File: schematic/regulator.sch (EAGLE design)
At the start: 26 parts, among them J1 COMM, J2 STOP_LIGHT, J3 ON/OFF, J4 BATTERY, J5 DRIVER, J6 DRIVER POWER, Q1 NMOSFETSOT23, Q2 NMOSFETSOT23, Q3 NMOSFETSOT23, Q4 IRFR3607PBF

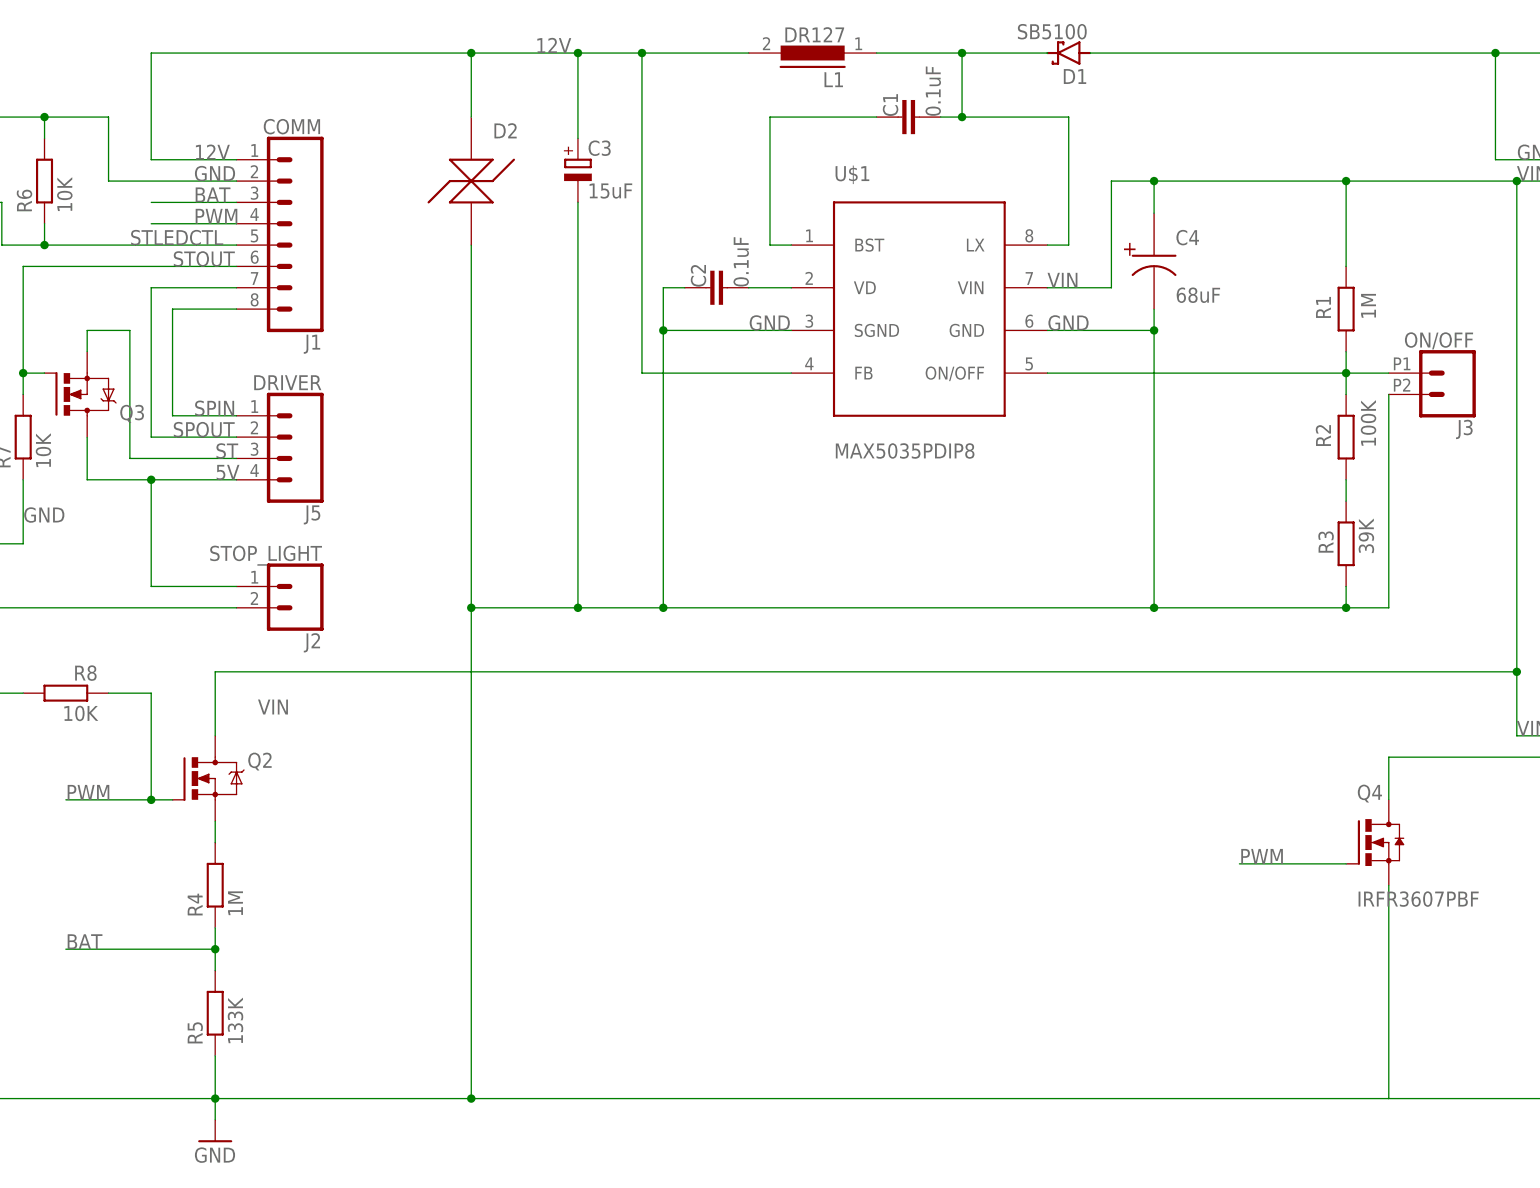
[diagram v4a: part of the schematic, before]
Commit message: Fix regulator schematics
- Fix regulator schematics, add missed voltage controll resistors
- Fix deprecated warnings for display
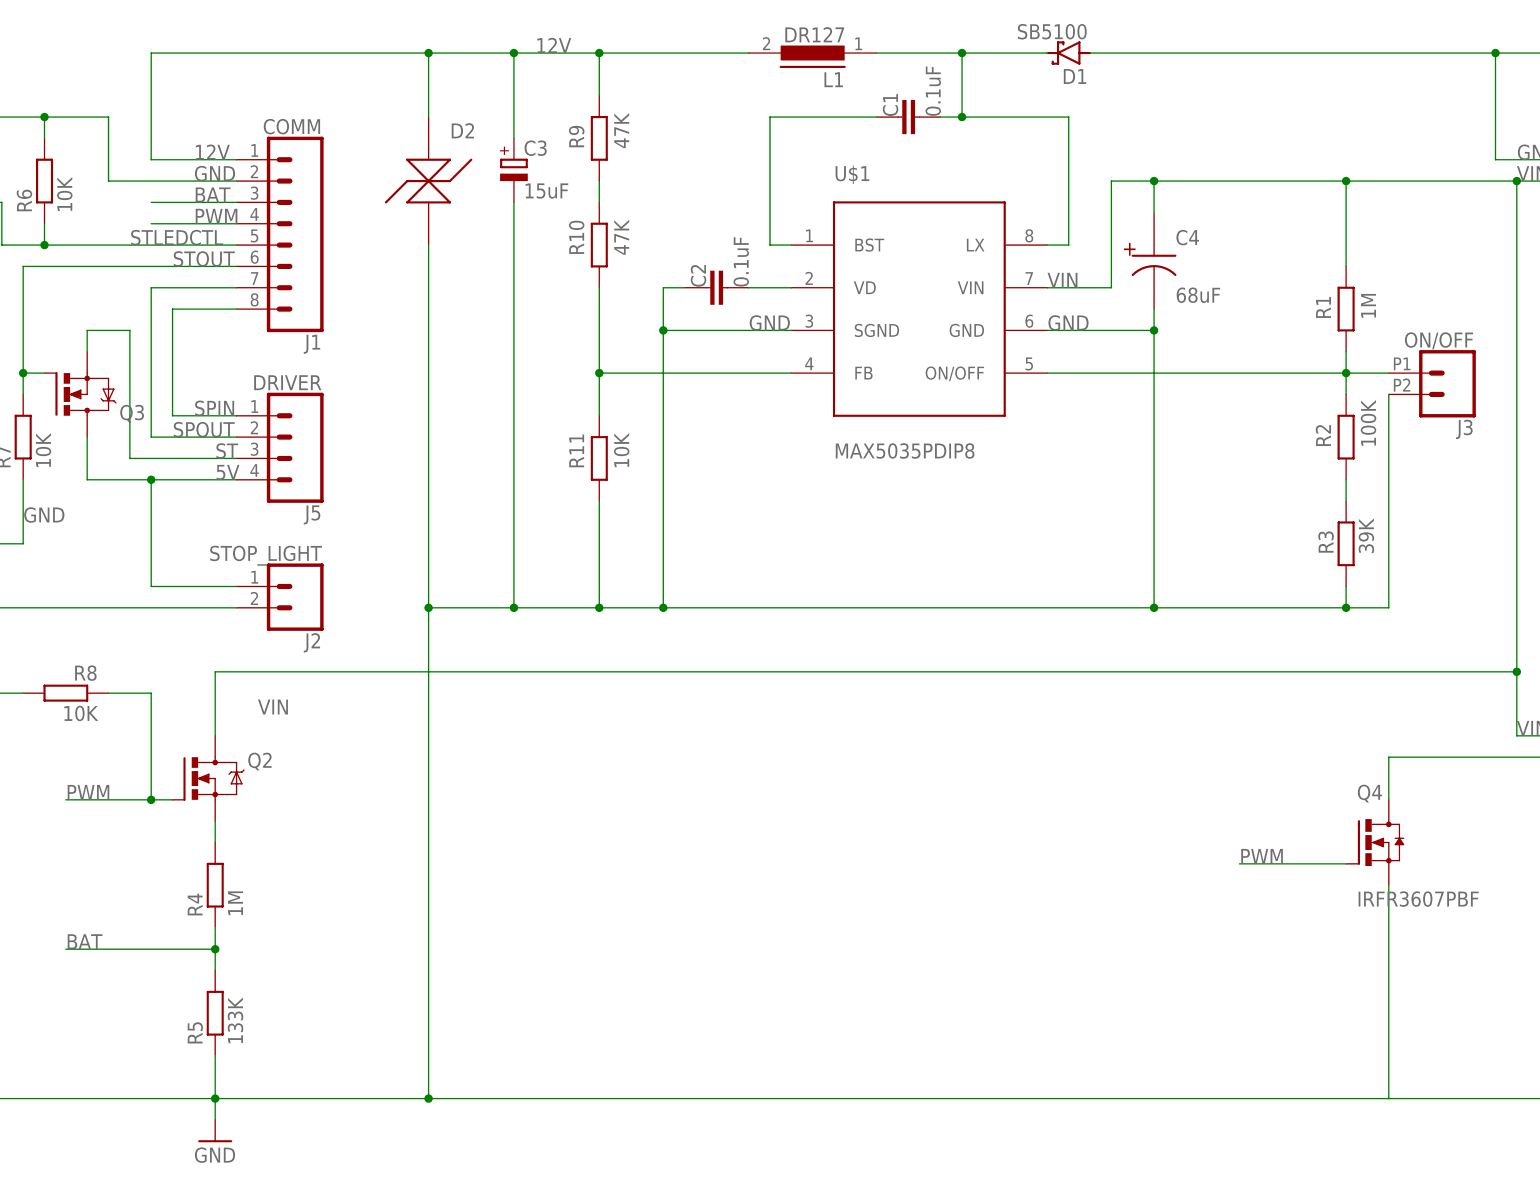
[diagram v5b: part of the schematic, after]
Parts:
- added R10, R9: 47K, eagle-ltspice:RR1206
- added R11: 10K, eagle-ltspice:RR1206
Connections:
- new net N$6: R10.1, R9.2
- new net N$9: R10.2, R11.1, U$1.FB
- net 12V: now also R9.1; no longer U$1.FB
- net GND: now also R11.2
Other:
- moved on the sheet: C3, D2
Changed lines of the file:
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@@
 <part name="J6" library="eScooter" deviceset="XT60" device="" value="DRIVER POWER"/>
 <part name="Q4" library="Transistor" library_urn="urn:adsk.eagle:library:14522416" deviceset="FQD13N06LTM" device="" package3d_urn="urn:adsk.eagle:package:10893256/5" value="IRFR3607PBF"/>
+<part name="R9" library="eagle-ltspice" library_urn="urn:adsk.eagle:library:217" deviceset="R" device="R1206" package3d_urn="urn:adsk.eagle:package:13301/1" value="47K"/>
+<part name="R10" library="eagle-ltspice" library_urn="urn:adsk.eagle:library:217" deviceset="R" device="R1206" package3d_urn="urn:adsk.eagle:package:13301/1" value="47K"/>
+<part name="R11" library="eagle-ltspice" library_urn="urn:adsk.eagle:library:217" deviceset="R" device="R1206" package3d_urn="urn:adsk.eagle:package:13301/1" value="10K"/>
 </parts>
 <sheets>
@@
 <attribute name="VALUE" x="111.76" y="104.14" size="1.778" layer="96" rot="R90"/>
 </instance>
-<instance part="C3" gate="G$1" x="91.44" y="119.38" smashed="yes">
-<attribute name="NAME" x="92.583" y="119.8626" size="1.778" layer="95"/>
-<attribute name="VALUE" x="92.583" y="114.7826" size="1.778" layer="96"/>
+<instance part="C3" gate="G$1" x="83.82" y="119.38" smashed="yes">
+<attribute name="NAME" x="84.963" y="119.8626" size="1.778" layer="95"/>
+<attribute name="VALUE" x="84.963" y="114.7826" size="1.778" layer="96"/>
 </instance>
 <instance part="R1" gate="G$1" x="182.88" y="101.6" smashed="yes" rot="R270">
@@
 <attribute name="VALUE" x="28.702" y="82.55" size="1.778" layer="96" rot="R90"/>
 </instance>
-<instance part="D2" gate="D$1" x="78.74" y="116.84" smashed="yes">
-<attribute name="NAME" x="81.28" y="121.92" size="1.778" layer="95"/>
+<instance part="D2" gate="D$1" x="73.66" y="116.84" smashed="yes">
+<attribute name="NAME" x="76.2" y="121.92" size="1.778" layer="95"/>
 </instance>
 <instance part="R8" gate="G$1" x="30.48" y="55.88" smashed="yes" rot="MR0">
@@
 <attribute name="NAME" x="184.15" y="43.18" size="1.778" layer="95"/>
 <attribute name="VALUE" x="184.15" y="30.48" size="1.778" layer="96"/>
+</instance>
+<instance part="R9" gate="G$1" x="93.98" y="121.92" smashed="yes" rot="R270">
+<attribute name="NAME" x="90.3986" y="120.65" size="1.778" layer="95" rot="MR90"/>
+<attribute name="VALUE" x="95.758" y="120.65" size="1.778" layer="96" rot="MR90"/>
+</instance>
+<instance part="R10" gate="G$1" x="93.98" y="109.22" smashed="yes" rot="R270">
+<attribute name="NAME" x="90.3986" y="107.95" size="1.778" layer="95" rot="MR90"/>
+<attribute name="VALUE" x="95.758" y="107.95" size="1.778" layer="96" rot="MR90"/>
+</instance>
+<instance part="R11" gate="G$1" x="93.98" y="83.82" smashed="yes" rot="R270">
+<attribute name="NAME" x="90.3986" y="82.55" size="1.778" layer="95" rot="MR90"/>
+<attribute name="VALUE" x="95.758" y="82.55" size="1.778" layer="96" rot="MR90"/>
 </instance>
 </instances>
@@
 <wire x1="187.96" y1="66.04" x2="182.88" y2="66.04" width="0.1524" layer="91"/>
 <wire x1="160.02" y1="66.04" x2="101.6" y2="66.04" width="0.1524" layer="91"/>
-<wire x1="101.6" y1="66.04" x2="91.44" y2="66.04" width="0.1524" layer="91"/>
-<wire x1="91.44" y1="66.04" x2="91.44" y2="114.3" width="0.1524" layer="91"/>
+<wire x1="101.6" y1="66.04" x2="93.98" y2="66.04" width="0.1524" layer="91"/>
+<wire x1="93.98" y1="66.04" x2="83.82" y2="66.04" width="0.1524" layer="91"/>
+<wire x1="83.82" y1="66.04" x2="83.82" y2="114.3" width="0.1524" layer="91"/>
 <pinref part="D1" gate="G$1" pin="A"/>
 <wire x1="152.4" y1="132.08" x2="200.66" y2="132.08" width="0.1524" layer="91"/>
@@
 <label x="203.2" y="119.38" size="1.778" layer="95"/>
 <pinref part="D2" gate="D$1" pin="P$2"/>
-<wire x1="78.74" y1="109.22" x2="78.74" y2="66.04" width="0.1524" layer="91"/>
-<wire x1="78.74" y1="66.04" x2="91.44" y2="66.04" width="0.1524" layer="91"/>
-<junction x="91.44" y="66.04"/>
-<wire x1="48.26" y1="7.62" x2="78.74" y2="7.62" width="0.1524" layer="91"/>
+<wire x1="73.66" y1="109.22" x2="73.66" y2="66.04" width="0.1524" layer="91"/>
+<wire x1="73.66" y1="66.04" x2="83.82" y2="66.04" width="0.1524" layer="91"/>
+<junction x="83.82" y="66.04"/>
+<wire x1="48.26" y1="7.62" x2="73.66" y2="7.62" width="0.1524" layer="91"/>
 <pinref part="R8" gate="G$1" pin="2"/>
 <wire x1="5.08" y1="55.88" x2="25.4" y2="55.88" width="0.1524" layer="91"/>
@@
 <wire x1="223.52" y1="132.08" x2="223.52" y2="7.62" width="0.1524" layer="91"/>
 <wire x1="223.52" y1="7.62" x2="187.96" y2="7.62" width="0.1524" layer="91"/>
-<wire x1="187.96" y1="7.62" x2="78.74" y2="7.62" width="0.1524" layer="91"/>
+<wire x1="187.96" y1="7.62" x2="73.66" y2="7.62" width="0.1524" layer="91"/>
 <wire x1="116.84" y1="99.06" x2="101.6" y2="99.06" width="0.1524" layer="91"/>
 <wire x1="101.6" y1="99.06" x2="101.6" y2="104.14" width="0.1524" layer="91"/>
@@
 <junction x="101.6" y="66.04"/>
 <label x="111.76" y="99.06" size="1.778" layer="95"/>
-<wire x1="78.74" y1="66.04" x2="78.74" y2="7.62" width="0.1524" layer="91"/>
-<junction x="78.74" y="66.04"/>
-<junction x="78.74" y="7.62"/>
+<wire x1="73.66" y1="66.04" x2="73.66" y2="7.62" width="0.1524" layer="91"/>
+<junction x="73.66" y="66.04"/>
+<junction x="73.66" y="7.62"/>
 <pinref part="C4" gate="G$1" pin="P$2"/>
 <pinref part="U$1" gate="G$1" pin="SGND"/>
@@
 <pinref part="Q4" gate="G$1" pin="S"/>
 <wire x1="187.96" y1="33.02" x2="187.96" y2="7.62" width="0.1524" layer="91"/>
+<pinref part="R11" gate="G$1" pin="2"/>
+<wire x1="93.98" y1="78.74" x2="93.98" y2="66.04" width="0.1524" layer="91"/>
+<junction x="93.98" y="66.04"/>
 </segment>
 </net>
@@
 <segment>
 <pinref part="L1" gate="G$1" pin="2"/>
-<wire x1="111.76" y1="132.08" x2="99.06" y2="132.08" width="0.1524" layer="91"/>
-<wire x1="99.06" y1="132.08" x2="99.06" y2="93.98" width="0.1524" layer="91"/>
-<wire x1="99.06" y1="93.98" x2="116.84" y2="93.98" width="0.1524" layer="91"/>
-<wire x1="99.06" y1="132.08" x2="91.44" y2="132.08" width="0.1524" layer="91"/>
-<junction x="99.06" y="132.08"/>
-<wire x1="91.44" y1="132.08" x2="91.44" y2="121.92" width="0.1524" layer="91"/>
-<junction x="91.44" y="132.08"/>
+<wire x1="111.76" y1="132.08" x2="93.98" y2="132.08" width="0.1524" layer="91"/>
+<wire x1="93.98" y1="132.08" x2="83.82" y2="132.08" width="0.1524" layer="91"/>
+<wire x1="83.82" y1="132.08" x2="83.82" y2="121.92" width="0.1524" layer="91"/>
+<junction x="83.82" y="132.08"/>
 <pinref part="C3" gate="G$1" pin="+"/>
 <label x="86.36" y="132.08" size="1.778" layer="95"/>
@@
 <wire x1="50.8" y1="119.38" x2="40.64" y2="119.38" width="0.1524" layer="91"/>
 <label x="45.72" y="119.38" size="1.778" layer="95"/>
-<wire x1="91.44" y1="132.08" x2="78.74" y2="132.08" width="0.1524" layer="91"/>
-<wire x1="78.74" y1="132.08" x2="40.64" y2="132.08" width="0.1524" layer="91"/>
+<wire x1="83.82" y1="132.08" x2="73.66" y2="132.08" width="0.1524" layer="91"/>
+<wire x1="73.66" y1="132.08" x2="40.64" y2="132.08" width="0.1524" layer="91"/>
 <wire x1="40.64" y1="132.08" x2="40.64" y2="119.38" width="0.1524" layer="91"/>
 <pinref part="D2" gate="D$1" pin="P$1"/>
-<wire x1="78.74" y1="132.08" x2="78.74" y2="124.46" width="0.1524" layer="91"/>
-<junction x="78.74" y="132.08"/>
-<pinref part="U$1" gate="G$1" pin="FB"/>
+<wire x1="73.66" y1="132.08" x2="73.66" y2="124.46" width="0.1524" layer="91"/>
+<junction x="73.66" y="132.08"/>
+<pinref part="R9" gate="G$1" pin="1"/>
+<wire x1="93.98" y1="132.08" x2="93.98" y2="127" width="0.1524" layer="91"/>
+<junction x="93.98" y="132.08"/>
 </segment>
 </net>
@@
 </segment>
 </net>
+<net name="N$6" class="0">
+<segment>
+<pinref part="R10" gate="G$1" pin="1"/>
+<pinref part="R9" gate="G$1" pin="2"/>
+<wire x1="93.98" y1="114.3" x2="93.98" y2="116.84" width="0.1524" layer="91"/>
+</segment>
+</net>
+<net name="N$9" class="0">
+<segment>
+<pinref part="U$1" gate="G$1" pin="FB"/>
+<wire x1="116.84" y1="93.98" x2="93.98" y2="93.98" width="0.1524" layer="91"/>
+<pinref part="R11" gate="G$1" pin="1"/>
+<wire x1="93.98" y1="93.98" x2="93.98" y2="88.9" width="0.1524" layer="91"/>
+<pinref part="R10" gate="G$1" pin="2"/>
+<wire x1="93.98" y1="93.98" x2="93.98" y2="104.14" width="0.1524" layer="91"/>
+<junction x="93.98" y="93.98"/>
+</segment>
+</net>
